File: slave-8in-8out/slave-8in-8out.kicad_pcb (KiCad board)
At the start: 2 copper layers, 61 x 72.4 mm, 6 parts, among them J1 Conn_01x06_Male, J3 Conn_01x06_Female, U1 MCP23017_SO

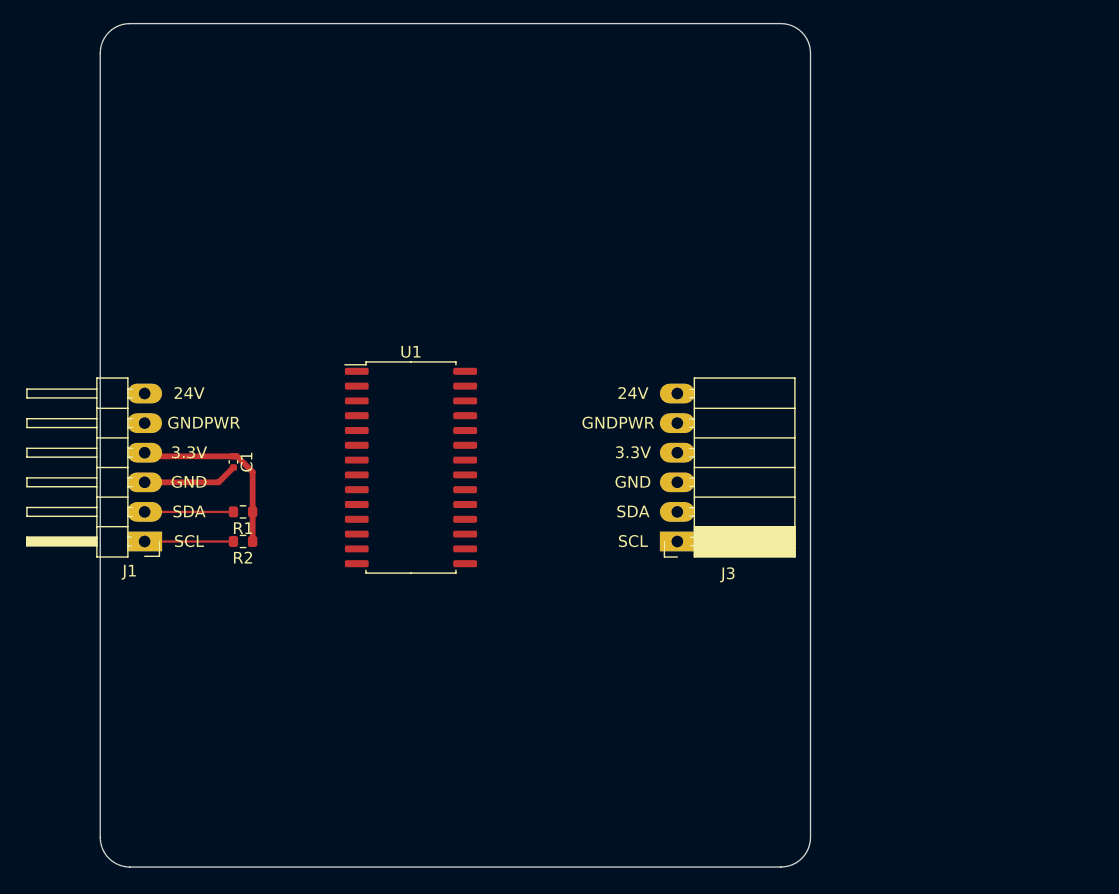
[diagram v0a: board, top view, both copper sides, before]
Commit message: add input optocouplers to slave-8in-8out
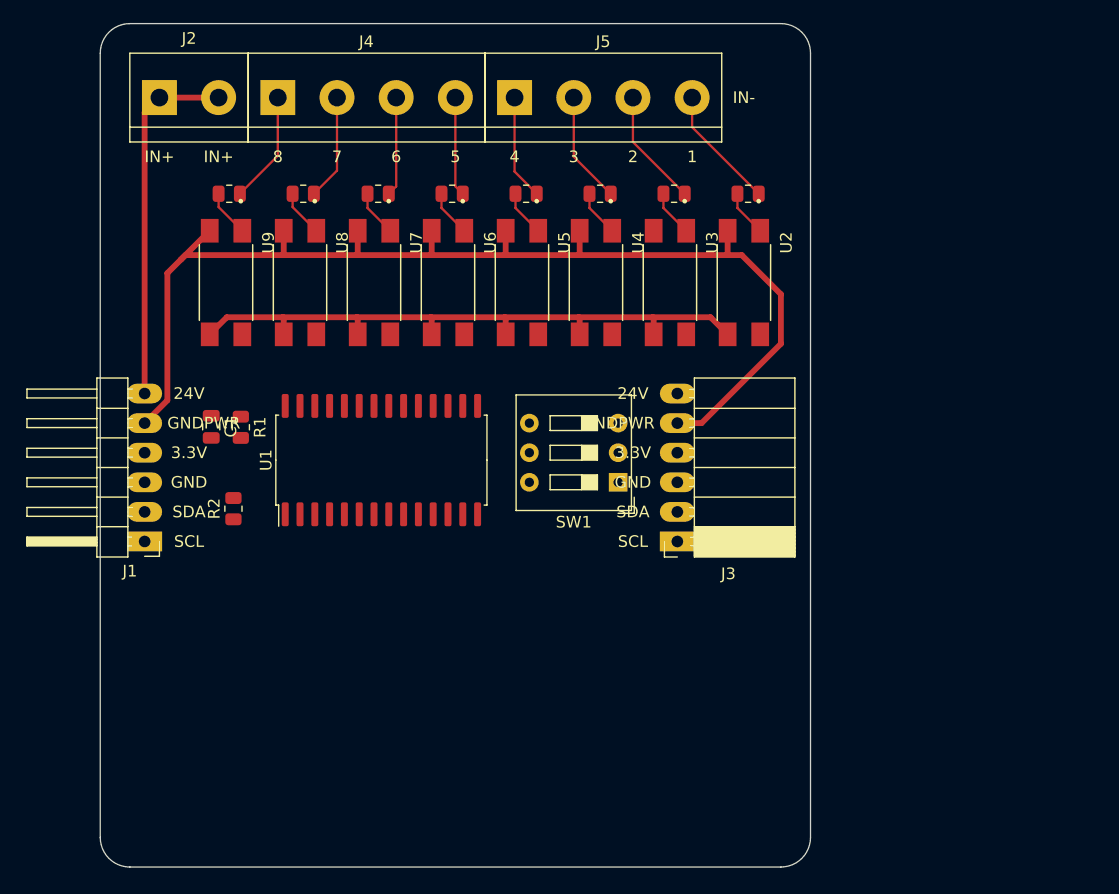
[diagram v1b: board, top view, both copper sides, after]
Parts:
- added J2: Screw_Terminal_01x02, TerminalBlock:TerminalBlock_bornier-2_P5.08mm, F.Cu at (68.6, 61.0)
- added J4: Screw_Terminal_01x04, TerminalBlock:TerminalBlock_bornier-4_P5.08mm, F.Cu at (78.7, 61.0)
- added J5: Screw_Terminal_01x04, TerminalBlock:TerminalBlock_bornier-4_P5.08mm, F.Cu at (99.1, 61.0)
- added R10: 4k7, Resistor_SMD:R_0805_2012Metric, F.Cu at (74.6, 69.2)
- added R3: 4k7, Resistor_SMD:R_0805_2012Metric, F.Cu at (119.1, 69.2)
- added R4: 4k7, Resistor_SMD:R_0805_2012Metric, F.Cu at (112.8, 69.2)
- added R5: 4k7, Resistor_SMD:R_0805_2012Metric, F.Cu at (106.4, 69.2)
- added R6: 4k7, Resistor_SMD:R_0805_2012Metric, F.Cu at (100.1, 69.2)
- added R7: 4k7, Resistor_SMD:R_0805_2012Metric, F.Cu at (93.7, 69.2)
- added R8: 4k7, Resistor_SMD:R_0805_2012Metric, F.Cu at (87.4, 69.2)
- added R9: 4k7, Resistor_SMD:R_0805_2012Metric, F.Cu at (80.9, 69.2)
- added SW1: SW_DIP_x03, Button_Switch_THT:SW_DIP_SPSTx03_Slide_9.78x9.8mm_W7.62mm_P2.54mm, F.Cu at (108.0, 94.0)
- added U2: EL817, jlcpcb:EL817, F.Cu at (118.7, 76.8)
- added U3: EL817, jlcpcb:EL817, F.Cu at (112.4, 76.8)
- added U4: EL817, jlcpcb:EL817, F.Cu at (106.0, 76.8)
- added U5: EL817, jlcpcb:EL817, F.Cu at (99.7, 76.8)
- added U6: EL817, jlcpcb:EL817, F.Cu at (93.3, 76.8)
- added U7: EL817, jlcpcb:EL817, F.Cu at (87.0, 76.8)
- added U8: EL817, jlcpcb:EL817, F.Cu at (80.6, 76.8)
- added U9: EL817, jlcpcb:EL817, F.Cu at (74.3, 76.8)
- C1: footprint Capacitor_SMD:C_0402_1005Metric -> Capacitor_SMD:C_0805_2012Metric
- R1, R2: footprint Resistor_SMD:R_0603_1608Metric -> Resistor_SMD:R_0805_2012Metric
- moved R1 7.26 mm to (75.6, 89.3), turned to 270 degrees
- moved C1 3.56 mm to (73.0, 89.2)
- moved R2 2.94 mm to (74.9, 96.2), turned to 90 degrees
- moved U1 2.62 mm to (87.6, 92.1), turned to 90 degrees
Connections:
- net Net-(U1-Pad1) renamed GPB0
- net Net-(U1-Pad2) renamed GPB1
- net Net-(U1-Pad3) renamed GPB2
- net Net-(U1-Pad4) renamed GPB3
- net Net-(U1-Pad5) renamed GPB4
- net Net-(U1-Pad6) renamed GPB5
- net Net-(U1-Pad7) renamed GPB6
- net Net-(U1-Pad8) renamed GPB7
- U1 pad 21: Net-(U1-Pad21) -> GPA0
- U1 pad 22: Net-(U1-Pad22) -> GPA1
- U1 pad 23: Net-(U1-Pad23) -> GPA2
- U1 pad 24: Net-(U1-Pad24) -> GPA3
- U1 pad 25: Net-(U1-Pad25) -> GPA4
- U1 pad 26: Net-(U1-Pad26) -> GPA5
- U1 pad 27: Net-(U1-Pad27) -> GPA6
- U1 pad 28: Net-(U1-Pad28) -> GPA7
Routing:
- net GNDPWR: track 0.00 -> 100.5 mm
- net GND: track 8.15 -> 54.6 mm
- net +24V: track 0.00 -> 31.0 mm
- net +3V3: track 15.9 -> 0.00 mm
- net I1: track 0.00 -> 10.6 mm
- net I2: track 0.00 -> 10.1 mm
- net I8: track 0.00 -> 9.60 mm
- net I3: track 0.00 -> 9.57 mm
- net I7: track 0.00 -> 9.08 mm
- net I4: track 0.00 -> 9.04 mm
- net I6: track 0.00 -> 8.52 mm
- net I5: track 0.00 -> 8.52 mm
- net SDA: track 7.62 -> 0.00 mm
- net SCL: track 7.62 -> 0.90 mm
- net Net-(R9-Pad1): track 0.00 -> 4.02 mm
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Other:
- board text added: "1"
- board text added: "2"
- board text added: "3"
- board text added: "4"
- board text added: "5"
- board text added: "6"
- board text added: "7"
- board text added: "8"
- board text added: "IN+"
- board text added: "IN-"

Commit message: add output to slave-8in-8out
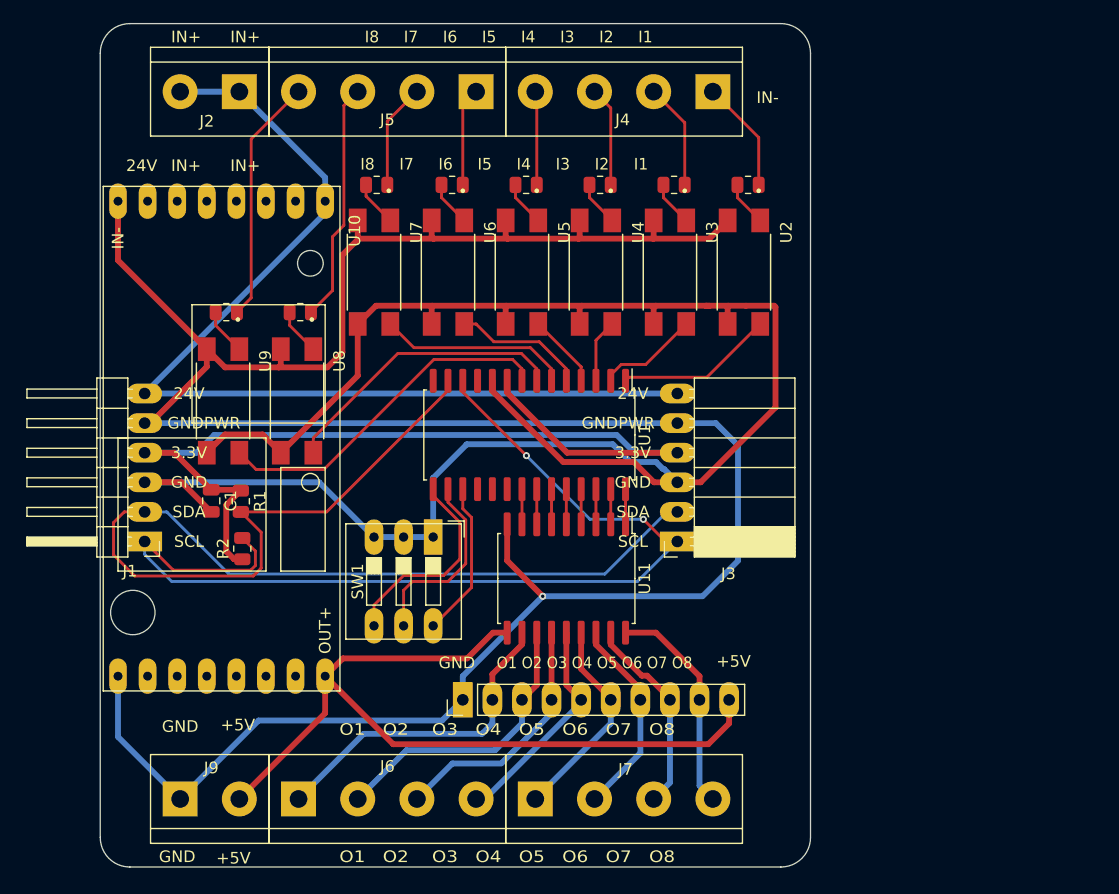
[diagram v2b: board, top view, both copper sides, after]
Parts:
- added J6: Screw_Terminal_01x04, TerminalBlock:TerminalBlock_bornier-4_P5.08mm, F.Cu at (80.5, 121.2)
- added J7: Screw_Terminal_01x04, TerminalBlock:TerminalBlock_bornier-4_P5.08mm, F.Cu at (100.8, 121.2)
- added J8: Conn_01x10_Male, Connector_PinHeader_2.54mm:PinHeader_1x10_P2.54mm_Vertical, F.Cu at (94.6, 112.6)
- added J9: Screw_Terminal_01x02, TerminalBlock:TerminalBlock_bornier-2_P5.08mm, F.Cu at (70.4, 121.2)
- added U10: LM2596-Board, boards:LM2596-Board, F.Cu at (73.9, 90.2)
- added U11: ULN2803A, Package_SO:SOIC-18W_7.5x11.6mm_P1.27mm, F.Cu at (103.5, 102.2)
- moved J4 37.3 mm to (116.1, 60.5), turned to 180 degrees
- moved SW1 16.6 mm to (92.1, 98.7), turned to 270 degrees
- moved U1 12.9 mm to (100.3, 89.9), turned to 270 degrees
- moved U9 10.2 mm to (74.0, 87.0)
- moved U8 10.2 mm to (80.4, 87.0)
- moved R10 10.2 mm to (74.3, 79.4)
- moved R9 10.2 mm to (80.7, 79.4)
- moved J2 6.88 mm to (75.4, 60.5), turned to 180 degrees
- moved R1 6.35 mm to (75.6, 95.6)
- moved C1 6.35 mm to (73.0, 95.6)
- moved R2 3.51 mm to (75.7, 99.7)
- moved J5 3.34 mm to (95.8, 60.5), turned to 180 degrees
- moved U2 0.89 mm to (118.7, 75.9)
- moved U3 0.89 mm to (112.4, 75.9)
- moved U4 0.89 mm to (106.0, 75.9)
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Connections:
- J4 pad 1: I8 -> I1
- J4 pad 2: I7 -> I2
- J4 pad 3: I6 -> I3
- J4 pad 4: I5 -> I4
- J5 pad 1: I4 -> I5
- J5 pad 2: I3 -> I6
- J5 pad 3: I2 -> I7
- J5 pad 4: I1 -> I8
- U2 pad 4: GPA0 -> GPB0
- U3 pad 4: GPA1 -> GPB1
- U4 pad 4: GPA2 -> GPB2
- U5 pad 4: GPA3 -> GPB3
- U6 pad 4: GPA4 -> GPB4
- U7 pad 4: GPA5 -> GPB5
- U8 pad 4: GPA6 -> GPB6
- U9 pad 4: GPA7 -> GPB7
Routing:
- net GNDPWR: track 100.5 -> 229.2 mm, vias 0 -> 1
- net GND: track 54.6 -> 168.1 mm
- net SDA: track 0.00 -> 98.1 mm
- net SCL: track 0.90 -> 87.4 mm, vias 0 -> 2
- net +3V3: track 0.00 -> 81.7 mm
- net +5V: track 0.00 -> 70.6 mm
- net +24V: track 31.0 -> 86.2 mm
- net GPB7: track 0.00 -> 30.1 mm
- net O1: track 0.00 -> 28.2 mm
- net O2: track 0.00 -> 25.1 mm
- net GPB6: track 0.00 -> 25.0 mm
- net O3: track 0.00 -> 21.5 mm
- net O4: track 0.00 -> 19.0 mm
- net O8: track 0.00 -> 18.9 mm
- net O5: track 0.00 -> 18.0 mm
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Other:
- net class Default: clearance 0.2 -> 0.25; trace_width 0.2 -> 0.25
- net class Power: clearance 0.2 -> 0.3
- rule trace_clearance: 0.2 -> 0.25
- board text added: "+5V"
- board text added: "I8 I7 I6 I5 I4 I3 I2 I1"
- board text added: "O1 O2 O3 O4 O5 O6 O7 O8"
- board text removed: "1"
- board text removed: "2"
- board text removed: "3"
- board text removed: "4"
- board text removed: "5"
- board text removed: "6"
- board text removed: "7"
- board text removed: "8"

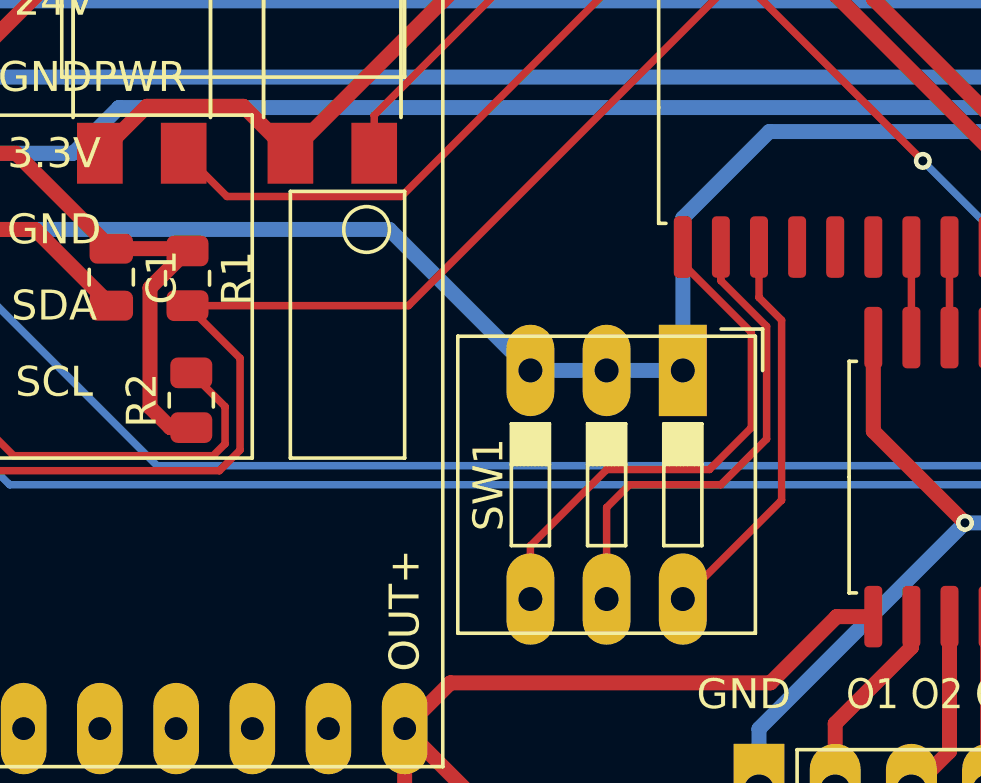
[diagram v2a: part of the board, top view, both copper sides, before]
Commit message: add pull-up resistor to mcp23017 reset pin
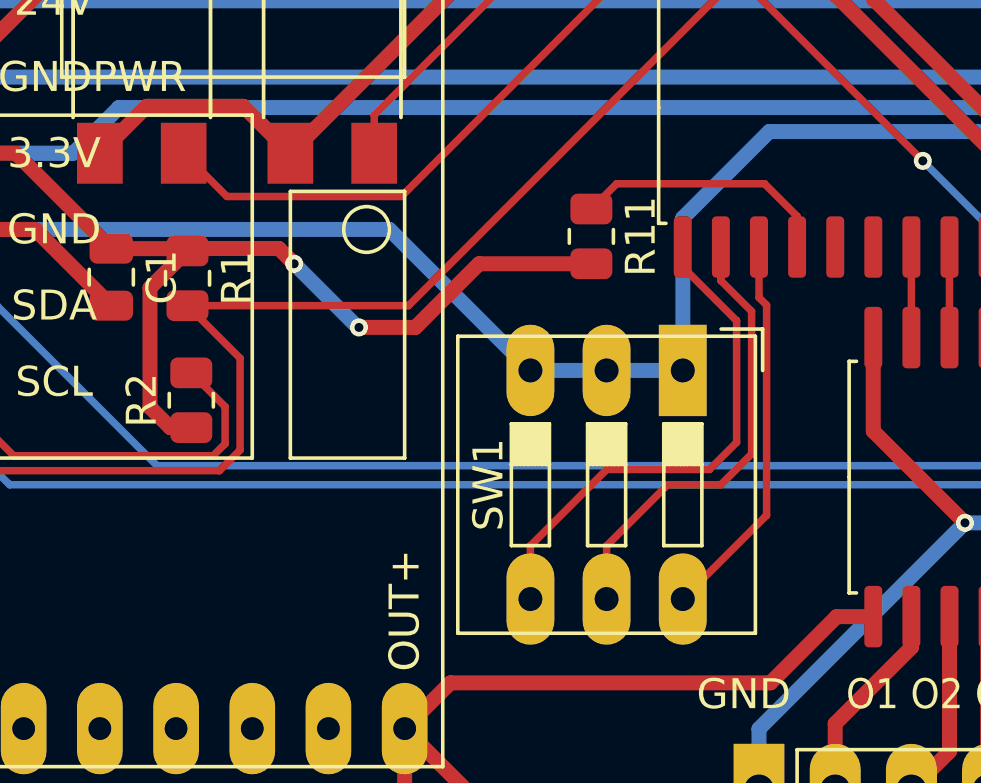
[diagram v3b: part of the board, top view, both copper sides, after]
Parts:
- added R11: 10k, Resistor_SMD:R_0805_2012Metric, F.Cu at (89.0, 94.2)
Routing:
- net +3V3: track 81.7 -> 97.2 mm, vias 0 -> 2
- net Net-(R11-Pad1): track 0.00 -> 8.68 mm
- net Net-(SW1-Pad5): track 16.4 -> 15.2 mm

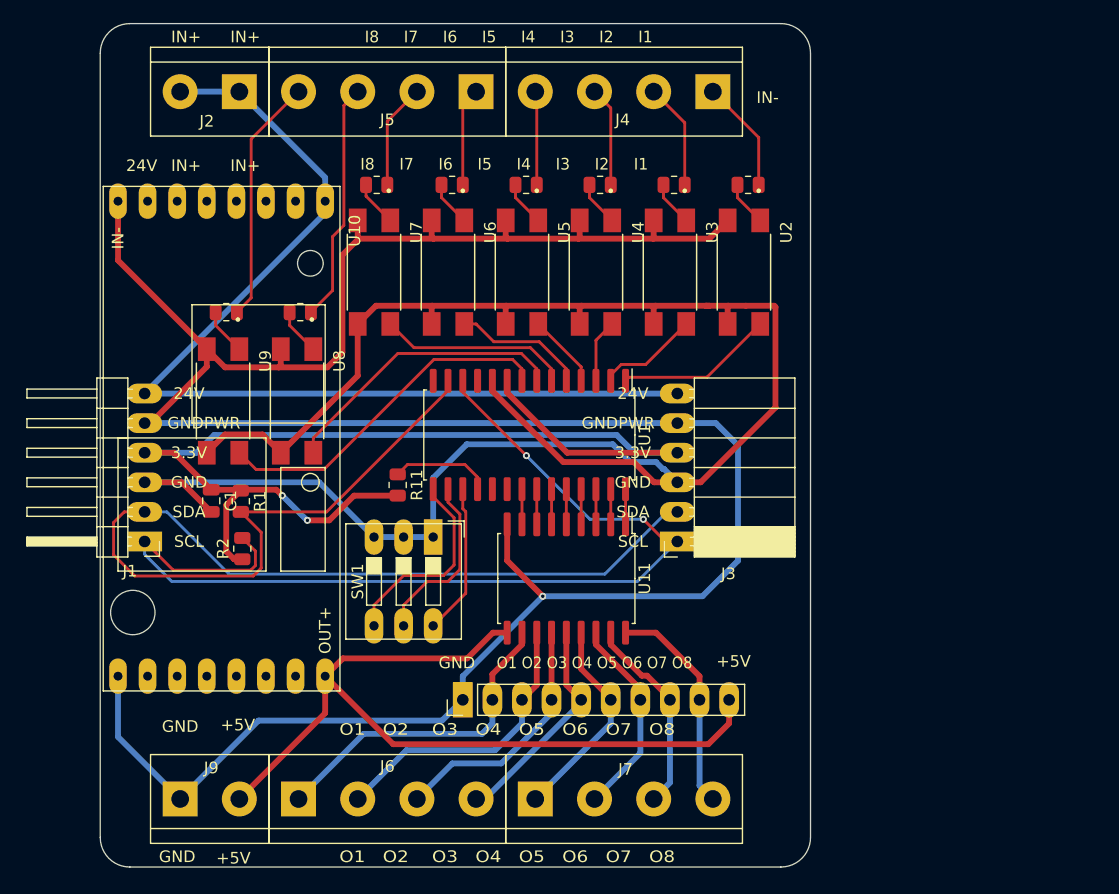
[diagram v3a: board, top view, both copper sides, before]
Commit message: move input/output connectors
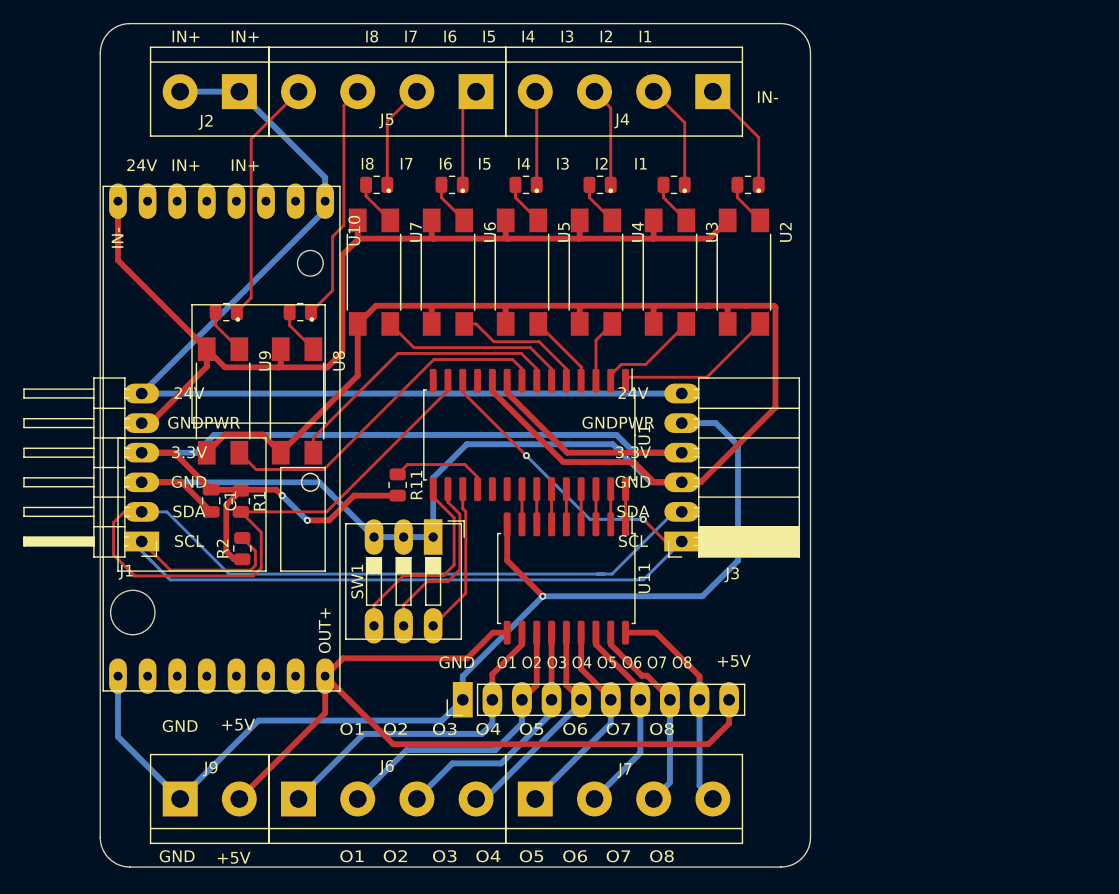
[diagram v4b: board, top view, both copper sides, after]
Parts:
- moved J3 0.38 mm to (113.4, 99.1)
- moved J1 0.25 mm to (67.1, 99.1)
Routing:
- net GNDPWR: track 229.2 -> 183.9 mm
- net SCL: track 87.4 -> 89.3 mm
- net +24V: track 86.2 -> 87.9 mm
- net +3V3: track 97.2 -> 98.5 mm
- net SDA: track 98.1 -> 99.2 mm
- net GND: track 168.1 -> 169.0 mm

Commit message: upgrade slave-8in-8out format
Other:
- net class Default removed
- net class Power removed
